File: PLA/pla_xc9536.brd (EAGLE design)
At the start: 18 x 36.2 mm, 5 parts

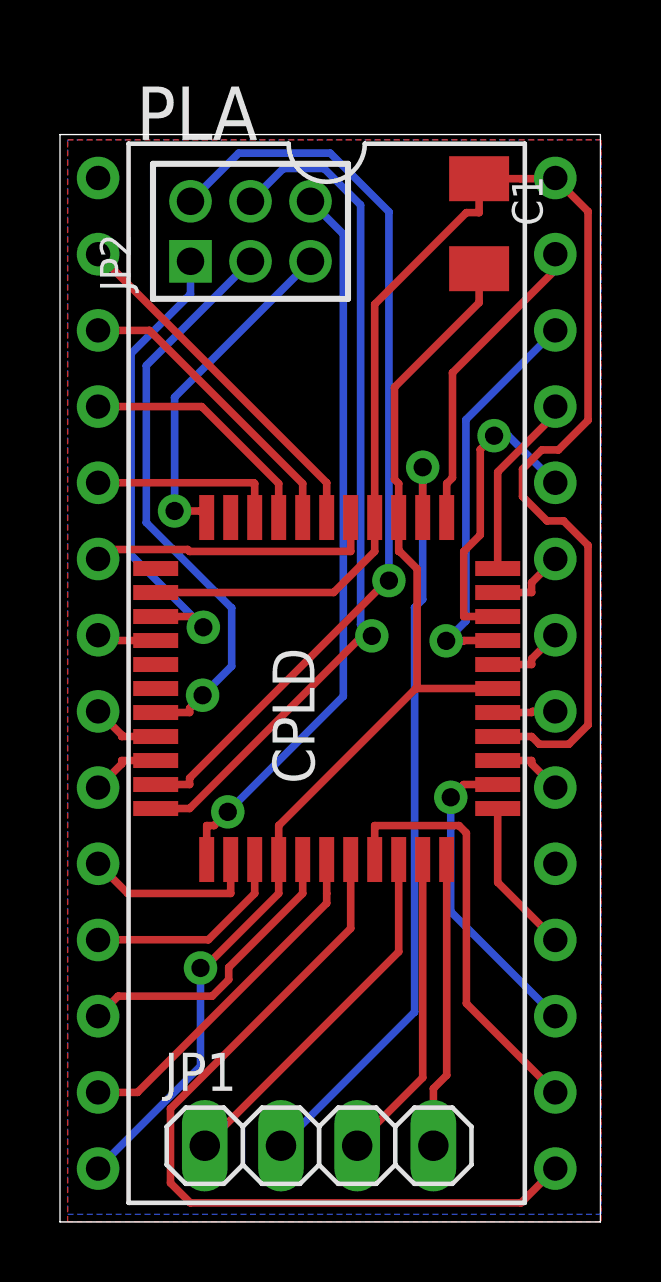
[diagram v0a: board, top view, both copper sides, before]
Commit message: updated schematic to remove floating pins
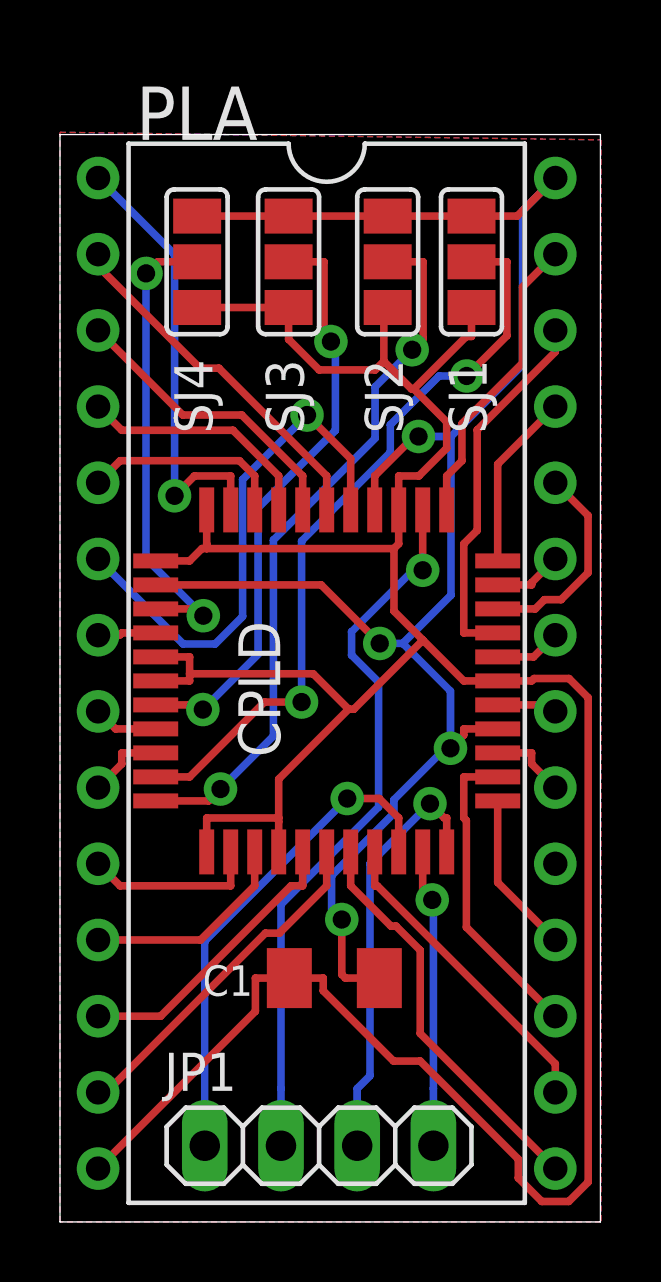
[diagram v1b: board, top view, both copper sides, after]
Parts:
- removed JP2: (no value), pinhead-new:2X03M
- added SJ1, SJ2, SJ3, SJ4: (no value), jumper:SJ_2
- moved C1 25.6 mm to (9.14, 8.13), turned to 180 degrees
- moved CPLD 0.25 mm to (8.89, 18.0)
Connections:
- removed net N$1: CPLD.43, JP2.2
- removed net N$2: CPLD.44, JP2.4
- removed net N$3: CPLD.1, JP2.6
- removed net N$4: CPLD.36, JP2.1
- removed net N$5: CPLD.33, JP2.5
- removed net N$6: CPLD.40, JP2.3
- new net 1: CPLD.43, SJ1.2
- new net 2: CPLD.44, SJ2.2
- new net 3: CPLD.40, SJ3.2
- new net 4: CPLD.36, SJ4.2
- net GND: now also CPLD.1, CPLD.33, CPLD.34, CPLD.38, CPLD.39, SJ1.1, SJ2.1, SJ3.1, SJ4.1
- net PLA1: now also CPLD.32
- net TCK: now also JP1.3; no longer JP1.4
- net TMS: now also JP1.4; no longer JP1.3
- net VCC: now also SJ1.3, SJ2.3, SJ3.3, SJ4.3
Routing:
- net GND: track 38.7 -> 102.0 mm, vias 1 -> 0
- net N$1: track 31.1 -> 0.00 mm, vias 1 -> 0
- net N$2: track 28.7 -> 0.00 mm, vias 1 -> 0
- net 1: track 0.00 -> 25.1 mm, vias 0 -> 2
- net N$3: track 24.4 -> 0.00 mm, vias 1 -> 0
- net 2: track 0.00 -> 23.9 mm, vias 0 -> 2
- net 3: track 0.00 -> 19.7 mm, vias 0 -> 2
- net N$6: track 19.4 -> 0.00 mm, vias 1 -> 0
- net N$4: track 15.8 -> 0.00 mm, vias 1 -> 0
- net 4: track 0.00 -> 15.7 mm, vias 0 -> 2
- net PLA1: track 0.00 -> 14.9 mm, vias 0 -> 1
- net CHAROM: track 26.8 -> 13.5 mm
- net N$5: track 11.4 -> 0.00 mm, vias 1 -> 0
- net VCC: track 49.1 -> 60.2 mm, vias 0 -> 4
- net CHAREN: track 9.71 -> 17.7 mm, vias 0 -> 1
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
